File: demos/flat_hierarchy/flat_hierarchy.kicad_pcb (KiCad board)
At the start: 2 copper layers, 160 x 99.1 mm, 64 parts, among them J1 DB9-FEMAL, P1 CONN_2, P2 SUPP28, P3 SUPP40, Q1 BC237, Q2 BC307, Q3 BC307, U1 24Cxx, U2 74HC125, U3 7805, U4 LT1373, U5 PIC_18_PINS, U6 PIC_8_PINS

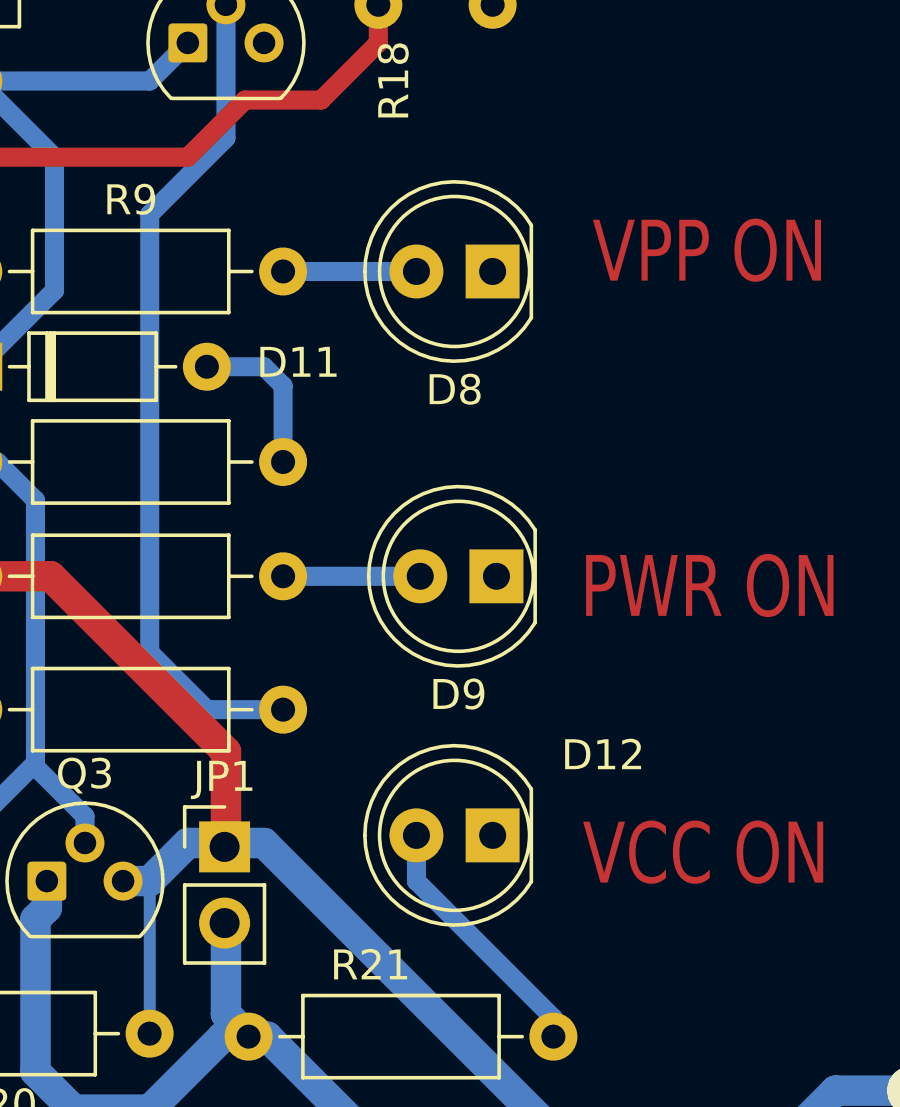
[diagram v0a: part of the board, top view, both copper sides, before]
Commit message: feat: update kicad to 9.0.0+dfsg-1
Signed-off-by: lhdjply <lhdjply@126.com>
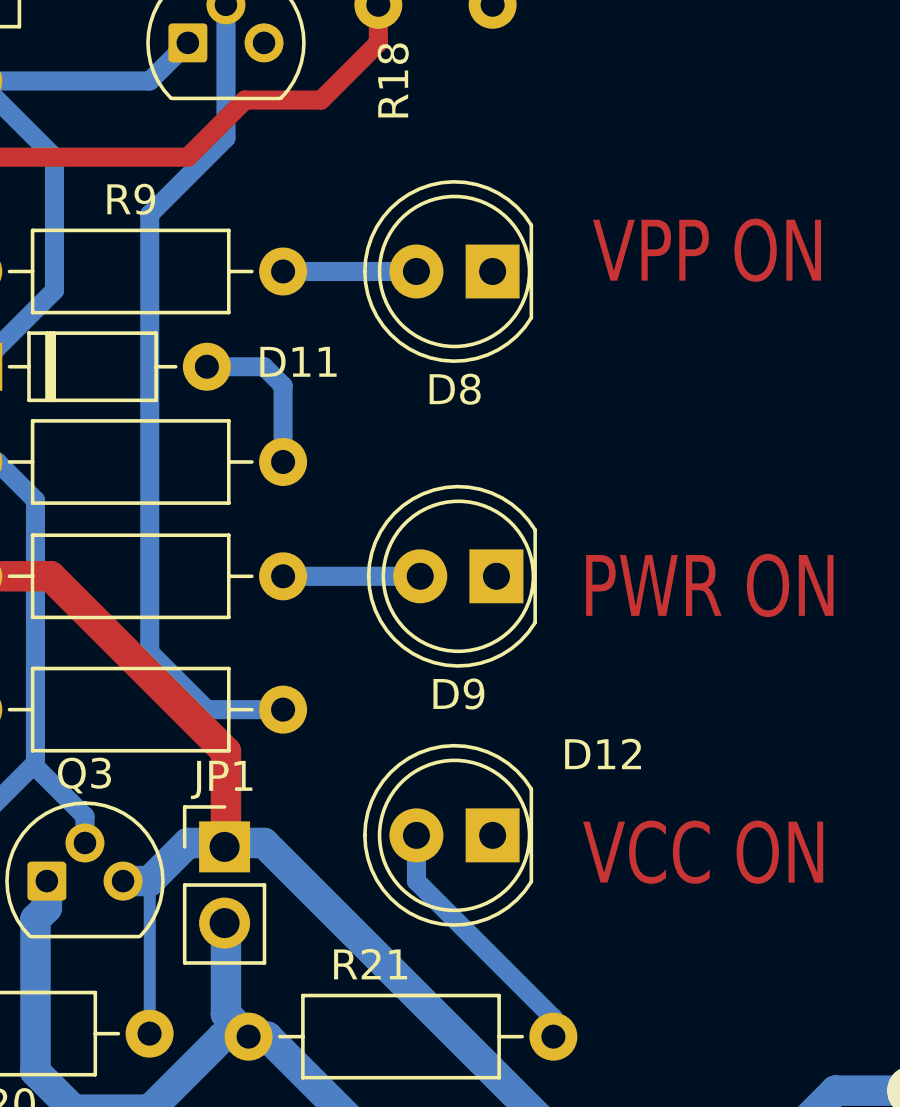
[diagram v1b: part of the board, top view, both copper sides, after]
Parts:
- C1, C2: footprint Capacitor_THT:CP_Axial_L18.0mm_D6.5mm_P25.00mm_Horizontal -> pic_programmer_fp:CP_Axial_L18.0mm_D6.5mm_P25.00mm_Horizontal
- C3: footprint Capacitor_THT:CP_Axial_L11.0mm_D6.0mm_P18.00mm_Horizontal -> pic_programmer_fp:CP_Axial_L11.0mm_D6.0mm_P18.00mm_Horizontal
- C4, C5, C6, C7, C8, C9: footprint Capacitor_THT:C_Disc_D5.1mm_W3.2mm_P5.00mm -> pic_programmer_fp:C_Disc_D5.1mm_W3.2mm_P5.00mm
- D1, D10: footprint Diode_THT:D_DO-35_SOD27_P12.70mm_Horizontal -> pic_programmer_fp:D_DO-35_SOD27_P12.70mm_Horizontal
- D12, D8, D9: footprint LED_THT:LED_D5.0mm -> pic_programmer_fp:LED_D5.0mm
- J1: footprint Connector_Dsub:DSUB-9_Female_Horizontal_P2.77x2.84mm_EdgePinOffset7.70mm_Housed_MountingHolesOffset9.12mm -> pic_programmer_fp:DSUB-9_Female_Horizontal_P2.77x2.84mm_EdgePinOffset7.70mm_Housed_MountingHolesOffset9.12mm
- JP1: footprint Connector_PinHeader_2.54mm:PinHeader_1x02_P2.54mm_Vertical -> pic_programmer_fp:PinHeader_1x02_P2.54mm_Vertical
- P1: footprint TerminalBlock_Altech:Altech_AK300_1x02_P5.00mm_45-Degree -> pic_programmer_fp:Altech_AK300_1x02_P5.00mm_45-Degree
- P2: footprint Package_DIP:DIP-28_W7.62mm_Socket_LongPads -> pic_programmer_fp:DIP-28_W7.62mm_Socket_LongPads
- P3: footprint Package_DIP:DIP-40_W15.24mm_Socket_LongPads -> pic_programmer_fp:DIP-40_W15.24mm_Socket_LongPads
- U1, U4, U6: footprint Package_DIP:DIP-8_W7.62mm_LongPads -> pic_programmer_fp:DIP-8_W7.62mm_LongPads
- U2: footprint Package_DIP:DIP-14_W7.62mm_LongPads -> pic_programmer_fp:DIP-14_W7.62mm_LongPads
- U5: footprint Package_DIP:DIP-18_W7.62mm_Socket_LongPads -> pic_programmer_fp:DIP-18_W7.62mm_Socket_LongPads
